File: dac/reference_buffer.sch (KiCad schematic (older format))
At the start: 21 parts, among them U1 OP27, U10 OP27

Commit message: More work on dac/power.sch and dac/reference_buffer.sch. Also, fixed comments in input/reference_buffer.sch
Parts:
- removed C2: 10nF, Capacitor_SMD:C_0805_2012Metric, symbol Device:C_Small
- removed C5, C6: 47uF, Capacitor_SMD:C_1210_3225Metric, symbol Device:C_Small
- removed R4: 2K, Resistor_SMD:R_0603_1608Metric, symbol Device:R_US
- removed R5: 68m, Resistor_SMD:R_1206_3216Metric, symbol Device:R_US
- TP5: value VREF -> VCOM
- gave numbers to parts that had none: 1
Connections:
- net VCOM: now also U10.2 (-), U10.6
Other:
- note added: "2.25 V\n(-2.75 V wrt. VCC)"
- note added: "The 5V reference comes in differentially so as to re-reference the voltage \nto local ground, minimizing effect of DC and low-frequency ground shifts.\nC1, C2 limit the bandwidth to 8 kHz. This bandwidth could be a lot lower,\nbut this would be awkward to implement because of the need for \ncapacitor matching to preserve CMRR. Instead, there are lowpass \nfilters downstream."
- note added: "The DAC VCOM pins are intended only for bypass on the internal reference, and\nin the normal application float at about 2.75V. But you can drive in a reference \non VCOM and get considerably reduced 1/f noise. A quirk is that this reference\nis with respect to the +5 VCC rail rather than ground.\n\nRather than re-referencing our output to some other +5 rail, we generate\nVCC by buffering our inco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"
- note added: "VREF comes right back \nas VCC -->"
- note removed: "Because the VCOM voltage is referenced to VCC we return the lowpass filter\nand output capacitors to VCC rather than ground. Likewise, the high end of\nthe voltage divider goes to VCC rather than VREF. But VCC is simply a\nbuffered version of VREF, and we want VCOM to track any noise on VCC.\n"
- note removed: "NEW"
- note removed: "The 15 Hz lowpass filter rejects HF crud\nin the incoming reference, and also noise\nfrom the diff amp itself (which operates a\nat noise gain of 2)."
- note removed: "The DAC VCOM pins are intended only for bypass on the internal reference, and\nin the normal application floats at about 2.75V. But you can drive in a reference \non VCOM and get considerably reduced 1/f noise. The trick\nis that this reference is with respect to the +5 VCC rail rather than ground.\nRather than re-referencing our output to some other +5 rail, we generate\nVCC by buffering our inc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"
- note removed: "The reference buffer receives the 5V reference from the edge connector\nand buffers it for the large capacitive load of the reference bypass caps. \nThe reference comes in differentially so as to re-reference the voltage to the gound\npresent on the input card, mimizing effect of DC and low-frequency ground shifts.\n\nThe loop bandwidth of the reference buffer is approximately 4.5 kHz\n#####\n."
- note removed: "VREF comes right back as VCC -->"
- moved on the sheet: C5, C6, C7, R5, R6, TP1, U2

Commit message: Much progress on the DAC card.  Schematic is complete, starting on placement.
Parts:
- removed C43, C44: 1uF, Capacitor_SMD:C_0805_2012Metric, symbol Device:C_Small
- removed U1, U10: OP27, Package_SO:SOIC-8_3.9x4.9mm_P1.27mm, symbol ilemt_input:opamp_single
- added U1: OPA2210, Package_SO:SOIC-8_3.9x4.9mm_P1.27mm, symbol ilemt_input:OPAMP_DUAL
- C1: Notes 2% C0G -> C0G, loose tolerence here
- C4: renamed from C41; Notes 2% C0G -> C0G, loose tolerence here
- TP1: renamed from TP5; footprint TestPoint:TestPoint_THTPad_D1.5mm_Drill0.7mm -> TestPoint:TestPoint_Keystone_5000-5004_Miniature
- renumbered C3 to C2, C4 to C3, C42 to C5, R36 to R10, R37 to R11, R6 to R12, R2 to R7, R1 to R8, R3 to R9
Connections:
- net V+: now also U1.8 (V+)
- net V-: now also U1.4 (V-)
- net VCOM: now also U1.5, U1.7
- net VREF: now also U1.1
- net U1B+: now reaches C5.2, R11.1, R12.2
- net U1B+: now also U1.6
- net GNDA renamed GND
- net U3+ renamed U1A+
- net U1A+: now also U1.2
- net U3- renamed U1A-
- net U1A-: now also U1.3
- net VCC renamed DAC_VCC
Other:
- note added: "2.25 V\n(-2.75 V wrt. DAC_VCC)"
- note added: "The DAC reference is negative wrt. VCC (see dac sheet), so we want VCOM to\ntrack any variation in VCC_DAC. Rather than re-referencing our output to some\nother +5 rail, we generate VCC_DAC by buffering our incoming +5 VREF (see power\nsheet). Then DAC_VCC is itself a low noise reference which can be used to\ngenerate VCOM.\n\nVCC tracking happens in the R11/R12/C5 network, which is a combined vo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"
- note added: "VREF comes right back \nas DAC_VCC -->"
- note removed: "2.25 V\n(-2.75 V wrt. VCC)"
- note removed: "The DAC VCOM pins are intended only for bypass on the internal reference, and\nin the normal application float at about 2.75V. But you can drive in a reference \non VCOM and get considerably reduced 1/f noise. A quirk is that this reference\nis with respect to the +5 VCC rail rather than ground.\n\nRather than re-referencing our output to some other +5 rail, we generate\nVCC by buffering our inco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"
- note removed: "VREF comes right back \nas VCC -->"

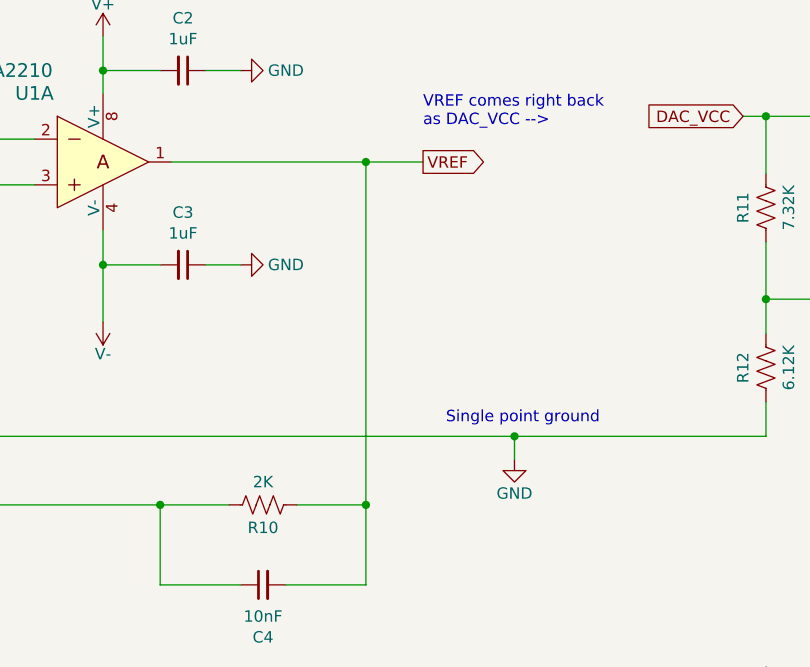
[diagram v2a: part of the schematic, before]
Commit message: DAC board is routed.  I also changed the digital interface to use a buffer (like I did on the input board) so that everything is buffered and we don't have multi-drop nets.
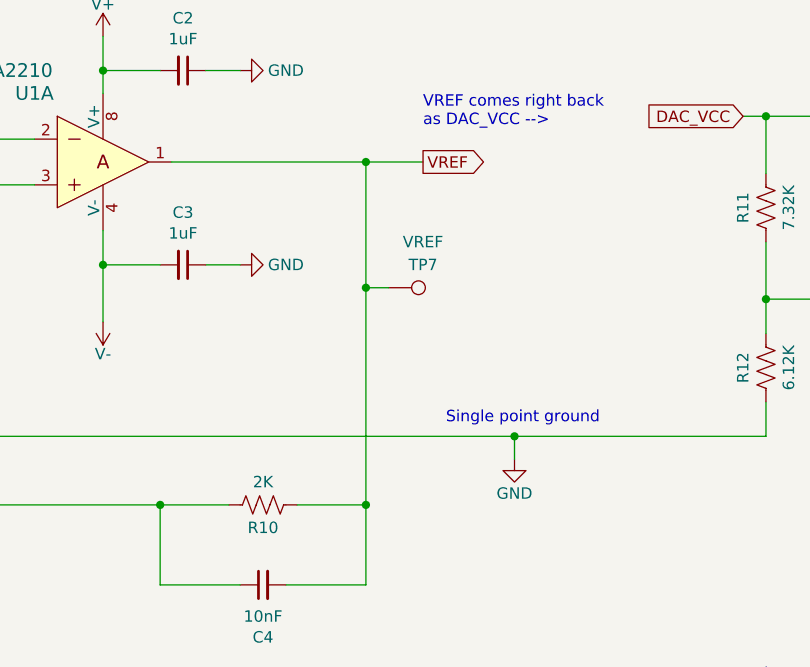
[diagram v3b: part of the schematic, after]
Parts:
- added TP7: VREF, TestPoint:TestPoint_Keystone_5000-5004_Miniature, symbol Connector:TestPoint
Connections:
- net VREF: now also TP7.1
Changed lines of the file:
@@
 Connection ~ 5200 4750
 Wire Wire Line
-	5200 4750 5200 3250
+	5200 4750 5200 3800
 Wire Wire Line
 	4650 5100 4300 5100
@@
 Text Label 7650 3850 0    50   ~ 0
 U1B+
+$Comp
+L Connector:TestPoint TP?
+U 1 1 5FA16C10
+P 5300 3800
+AR Path="/5DFCF14D/5DA78AA2/5FA16C10" Ref="TP?"  Part="1"
+AR Path="/5DFCF14D/5E295469/5FA16C10" Ref="TP?"  Part="1"
+AR Path="/5DFCF14D/5E195558/5FA16C10" Ref="TP?"  Part="1"
+AR Path="/5E2EB92B/5FA16C10" Ref="TP?"  Part="1"
+AR Path="/5E624B3C/5E2EB92B/5FA16C10" Ref="TP?"  Part="1"
+AR Path="/5EBEDCCA/5FA16C10" Ref="TP?"  Part="1"
+AR Path="/5F7CD5F5/5FA16C10" Ref="TP7"  Part="1"
+F 0 "TP7" V 5200 3950 50  0000 C CNN
+F 1 "VREF" V 5100 3950 50  0000 C CNN
+F 2 "TestPoint:TestPoint_Keystone_5000-5004_Miniature" H 5500 3800 50  0001 C CNN
+F 3 "~" H 5500 3800 50  0001 C CNN
+F 4 "Do Not Populate" H 5300 3800 50  0001 C CNN "Description"
+F 5 "DNP" H 5300 3800 50  0001 C CNN "MPN"
+	1    5300 3800
+	0    1    1    0
+$EndComp
+Wire Wire Line
+	5300 3800 5200 3800
+Connection ~ 5200 3800
+Wire Wire Line
+	5200 3800 5200 3250
 $EndSCHEMATC

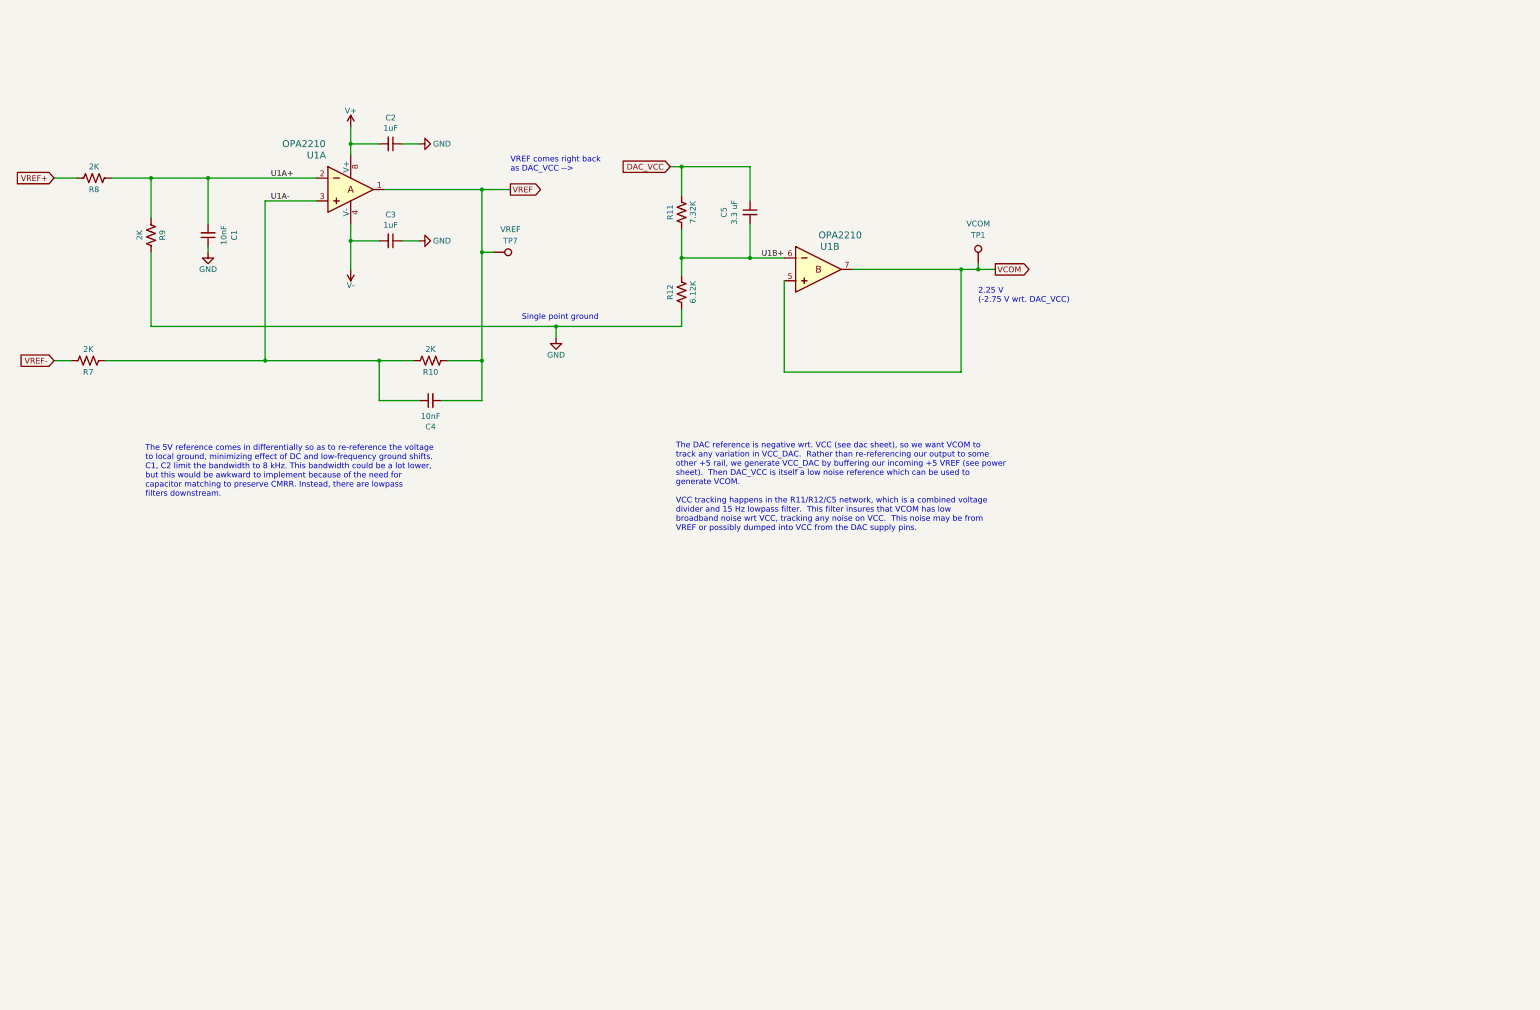
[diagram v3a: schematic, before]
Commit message: Everything seems ready to go for the DAC board.  Made my BOM and checked it twice. Checked footprints of new components and fixed J5, R7-R10.
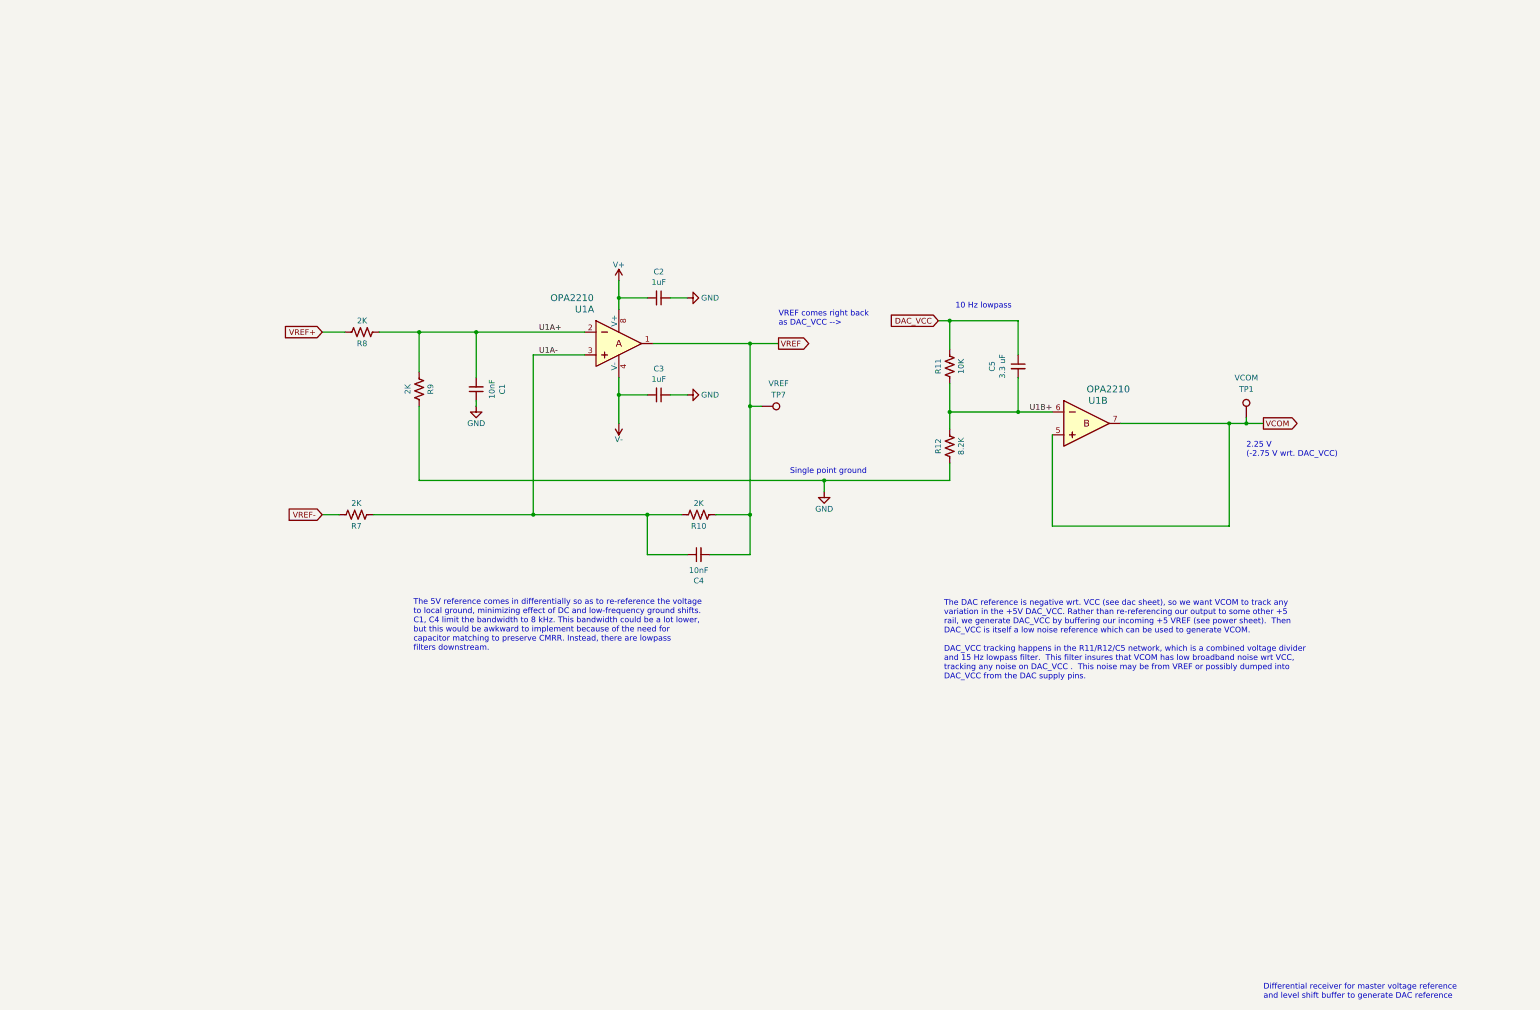
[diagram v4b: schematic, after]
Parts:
- C1, C4: DK line 14 -> I.14
- C2, C3: DK line 27 -> I.27
- C5: DK line (none) -> M.6; Description (none) -> CAP FILM 3.3UF 5% 63VDC RADIAL
- R10, R7, R8, R9: footprint Resistor_SMD:R_0603_1608Metric -> Resistor_SMD:R_0805_2012Metric; DK line 17 -> I.17
- R11: value 7.32K -> 10K; DK line (none) -> I.56; Description (none) -> RES SMD 10K OHM 0.1% 1/10W 0603; Digikey (none) -> P10KDBCT-ND; MPN (none) -> ERA-3AEB103V; Manufacturer (none) -> Panasonic Electronic Components
- R12: value 6.12K -> 8.2K; DK line (none) -> D.38; Description (none) -> RES SMD 8.2K OHM 0.5% 1/10W 0603; Digikey (none) -> P123782CT-ND; MPN (none) -> ERA-3AED822V; Manufacturer (none) -> Panasonic Electronic Components
- TP1, TP7: Description Do Not Populate -> Optional Keystone 5000-5004; Manufacturer (none) -> Keystone Electronics
- U1: DK line (none) -> D.1; Digikey (none) -> 296-OPA2210IDGKRCT-ND; MPN (none) -> OPA2210IDGKR; Manufacturer (none) -> Texas Instruments
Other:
- note added: "10 Hz lowpass"
- note added: "Differential receiver for master voltage reference\nand level shift buffer to generate DAC reference"
- note added: "The 5V reference comes in differentially so as to re-reference the voltage \nto local ground, minimizing effect of DC and low-frequency ground shifts.\nC1, C4 limit the bandwidth to 8 kHz. This bandwidth could be a lot lower,\nbut this would be awkward to implement because of the need for \ncapacitor matching to preserve CMRR. Instead, there are lowpass \nfilters downstream."
- note added: "The DAC reference is negative wrt. VCC (see dac sheet), so we want VCOM to track any\nvariation in the +5V DAC_VCC. Rather than re-referencing our output to some other +5\nrail, we generate DAC_VCC by buffering our incoming +5 VREF (see power sheet). Then\nDAC_VCC is itself a low noise reference which can be used to generate VCOM.\n\nDAC_VCC tracking happens in the R11/R12/C5 network, which is a 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"
- note removed: "The 5V reference comes in differentially so as to re-reference the voltage \nto local ground, minimizing effect of DC and low-frequency ground shifts.\nC1, C2 limit the bandwidth to 8 kHz. This bandwidth could be a lot lower,\nbut this would be awkward to implement because of the need for \ncapacitor matching to preserve CMRR. Instead, there are lowpass \nfilters downstream."
- note removed: "The DAC reference is negative wrt. VCC (see dac sheet), so we want VCOM to\ntrack any variation in VCC_DAC. Rather than re-referencing our output to some\nother +5 rail, we generate VCC_DAC by buffering our incoming +5 VREF (see power\nsheet). Then DAC_VCC is itself a low noise reference which can be used to\ngenerate VCOM.\n\nVCC tracking happens in the R11/R12/C5 network, which is a combined vo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"
- moved on the sheet: C1, C2, C3, C4, C5, R10, R11, R12, R7, R8, R9, TP1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

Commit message: Schematic revision for DAC board, compensation tweaks in lv_regs.
Opamp +/- pins were swapped in reference_buffer.sch as side effect of the symbol change from using a dual opamp.

lv_regs files.  The compensation components were (CTUNE/RTUNE) were quite wrong, and everything oscillated like crazy. The positive regulators are fine with no compensation, and the negative regulator benefits from a bit.
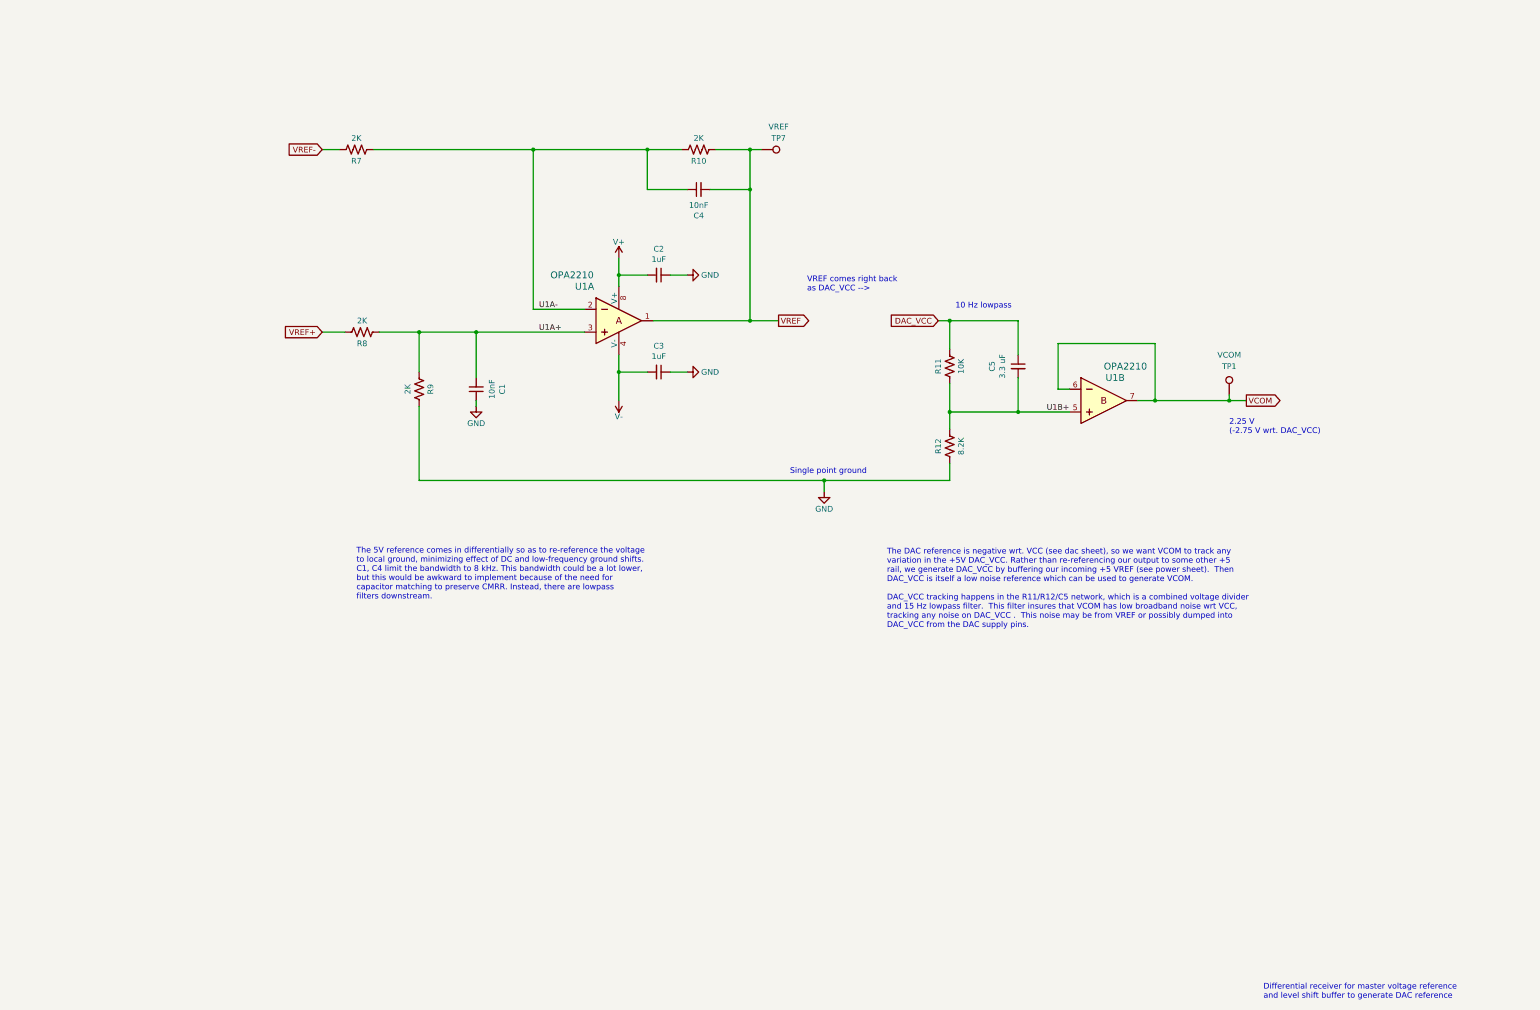
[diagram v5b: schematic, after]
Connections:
- net U1A+: now also U1.3; no longer U1.2
- net U1A-: now also U1.2; no longer U1.3
- net U1B+: now also U1.5; no longer U1.6
- net VCOM: now also U1.6; no longer U1.5
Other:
- moved on the sheet: C2, C3, C4, R10, R7, TP1, TP7, U1A, U1B
